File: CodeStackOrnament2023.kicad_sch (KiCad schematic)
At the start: 22 parts, among them SW1 SW_SPST, U1 NE555D, U2 4040

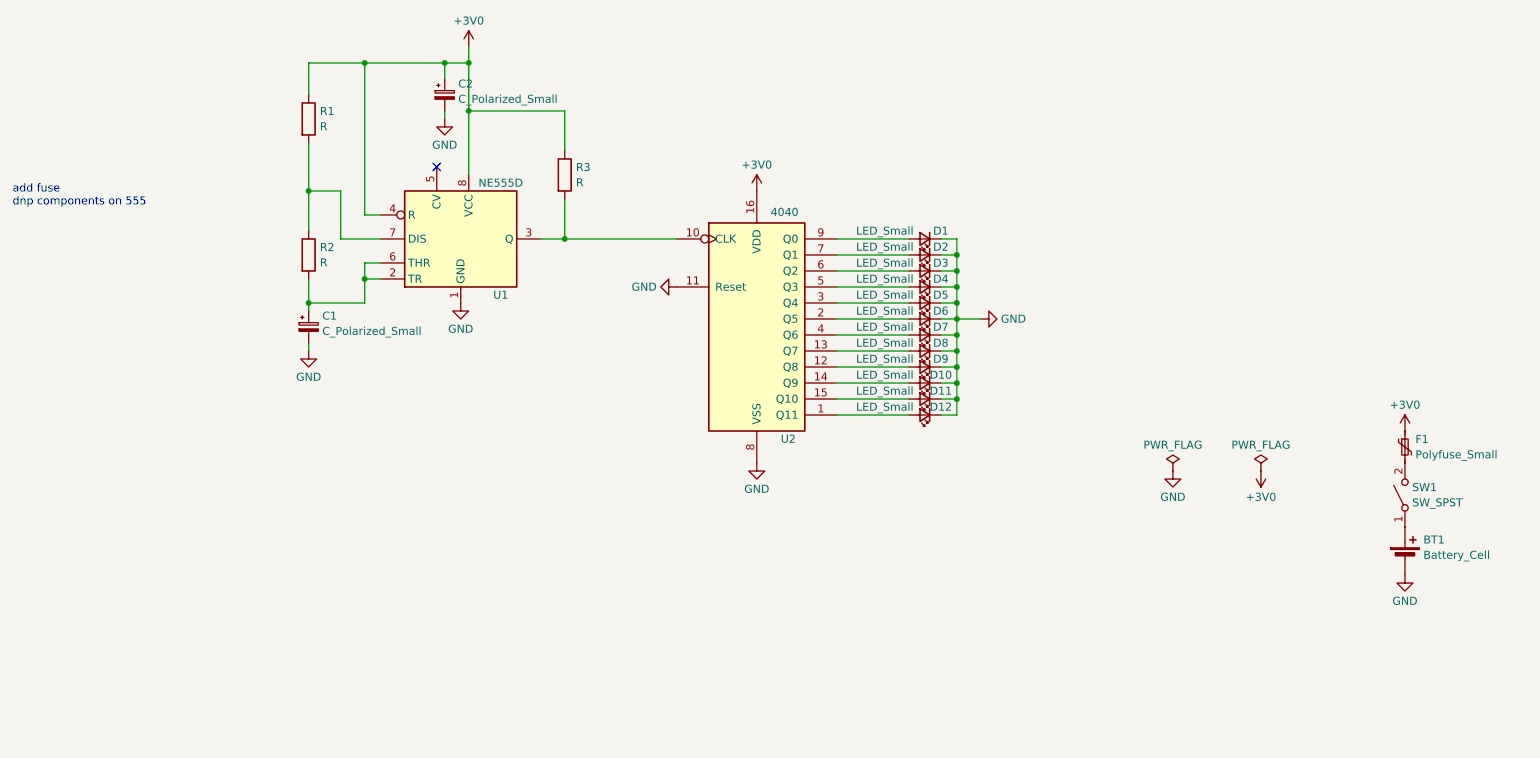
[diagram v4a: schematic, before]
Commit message: spice and footprint models. refactoring power supply.
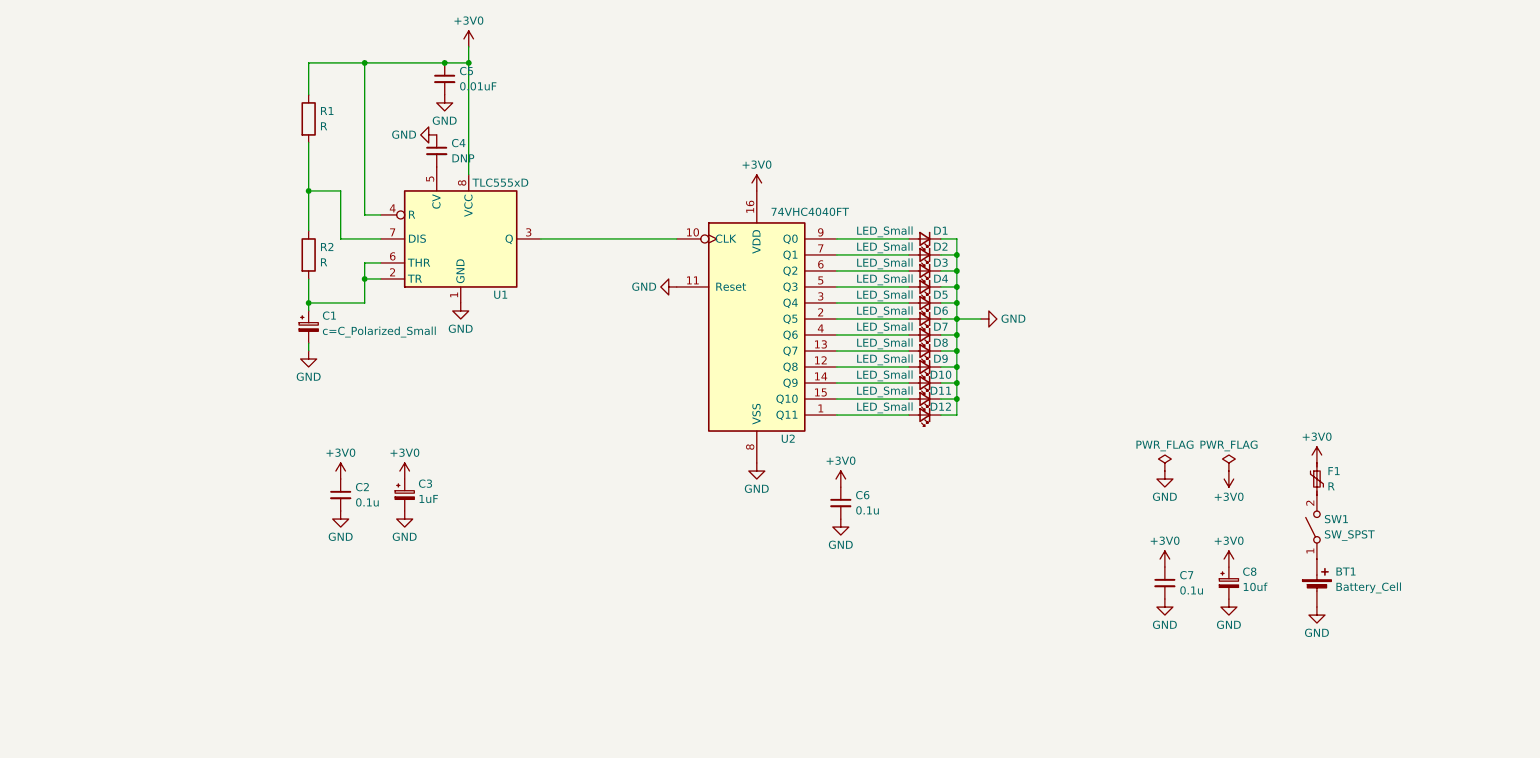
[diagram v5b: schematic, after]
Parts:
- removed C2: C_Polarized_Small, Capacitor_SMD:C_0805_2012Metric, symbol Device:C_Polarized_Small
- removed R3: R, Resistor_SMD:R_0805_2012Metric, symbol Device:R
- added C2, C6, C7: 0.1u, Capacitor_SMD:C_0805_2012Metric, symbol Device:C_Small
- added C3: 1uF, Capacitor_SMD:C_0805_2012Metric, symbol Device:C_Polarized_Small
- added C4: DNP, Capacitor_SMD:C_0805_2012Metric, symbol Device:C_Small
- added C5: 0.01uF, Capacitor_SMD:C_0805_2012Metric, symbol Device:C_Small
- added C8: 10uf, Capacitor_SMD:C_0805_2012Metric, symbol Device:C_Polarized_Small
- BT1: footprint CodeStackOrnament2023Footprints:2466_AAA_HOLDER -> CodeStackOrnament2023Footprints:BAT_2468
- C1: value C_Polarized_Small -> ${SIM.PARAMS}
- F1: value Polyfuse_Small -> R; footprint (none) -> Resistor_SMD:R_0805_2012Metric
- U1: value NE555D -> TLC555xD; footprint Package_SO:SOIC-8_3.9x4.9mm_P1.27mm -> CodeStackOrnament2023Footprints:TLC555_SOIC
- U2: value 4040 -> 74VHC4040FT
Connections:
- net +3V0: now also C2.1, C3.1, C5.1, C6.1, C7.1, C8.1
- net GND: now also C2.2, C3.2, C4.1, C5.2, C6.2, C7.2, C8.2
- net at U1.5 (CV): now also C4.2
- no-connect marks 1 -> 0
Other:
- note removed: "add fuse dnp components on 555"
- moved on the sheet: BT1, F1, SW1

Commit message: starting board design
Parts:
- removed C5: 0.01uF, Capacitor_SMD:C_0805_2012Metric, symbol Device:C_Small
- C1: value ${SIM.PARAMS} -> 10uF
- R1, R2: value R -> 8k
- renumbered C6 to C5, C7 to C6, C8 to C7
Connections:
- net at BT1.1 (+): now also SW1.2 (A); no longer SW1.1 (A)
- net at F1.2: now also SW1.3 (B); no longer SW1.2 (B)

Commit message: board layout
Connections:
- net +3V0: now also SW1.3 (B); no longer F1.1
- net at SW1.2 (A): now also F1.1; no longer BT1.1 (+)
- net at F1.2: now also BT1.1 (+); no longer SW1.3 (B)
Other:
- moved on the sheet: F1, SW1
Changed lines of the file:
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@@
     )
   )
-  (symbol (lib_id "Switch:SW_SPST") (at 229.87 97.79 90) (unit 1)
-    (in_bom yes) (on_board yes) (dnp no) (fields_autoplaced)
-    (property "Reference" "SW1" (at 231.013 96.5779 90)
+  (symbol (lib_id "Switch:SW_SPST") (at 229.87 92.71 90) (unit 1)
+    (in_bom yes) (on_board yes) (dnp no) (fields_autoplaced)
+    (property "Reference" "SW1" (at 231.013 91.4979 90)
       (effects (font (size 1.27 1.27)) (justify right))
     )
-    (property "Value" "SW_SPST" (at 231.013 99.0021 90)
+    (property "Value" "SW_SPST" (at 231.013 93.9221 90)
       (effects (font (size 1.27 1.27)) (justify right))
     )
-    (property "Footprint" "CodeStackOrnament2023Footprints:JS202011SCQN_SWITCH" (at 229.87 97.79 0)
-      (effects (font (size 1.27 1.27)) hide)
-    )
-    (property "Datasheet" "~" (at 229.87 97.79 0)
-      (effects (font (size 1.27 1.27)) hide)
-    )
-    (property "Sim.Device" "SW" (at 229.87 97.79 0)
-      (effects (font (size 1.27 1.27)) hide)
-    )
-    (property "Sim.Type" "V" (at 229.87 97.79 0)
-      (effects (font (size 1.27 1.27)) hide)
-    )
-    (property "Sim.Pins" "1=ctrl- 2=ctrl+" (at 229.87 97.79 0)
+    (property "Footprint" "CodeStackOrnament2023Footprints:JS202011SCQN_SWITCH" (at 229.87 92.71 0)
+      (effects (font (size 1.27 1.27)) hide)
+    )
+    (property "Datasheet" "~" (at 229.87 92.71 0)
+      (effects (font (size 1.27 1.27)) hide)
+    )
+    (property "Sim.Device" "SW" (at 229.87 92.71 0)
+      (effects (font (size 1.27 1.27)) hide)
+    )
+    (property "Sim.Type" "V" (at 229.87 92.71 0)
+      (effects (font (size 1.27 1.27)) hide)
+    )
+    (property "Sim.Pins" "1=ctrl- 2=ctrl+" (at 229.87 92.71 0)
       (effects (font (size 1.27 1.27)) hide)
     )
@@
     )
   )
-  (symbol (lib_id "Device:Polyfuse_Small") (at 229.87 90.17 0) (unit 1)
-    (in_bom yes) (on_board yes) (dnp no) (fields_autoplaced)
-    (property "Reference" "F1" (at 231.521 88.9579 0)
-      (effects (font (size 1.27 1.27)) (justify left))
-    )
-    (property "Value" "R" (at 231.521 91.3821 0)
-      (effects (font (size 1.27 1.27)) (justify left))
-    )
-    (property "Footprint" "Resistor_SMD:R_0805_2012Metric" (at 231.14 95.25 0)
+  (symbol (lib_id "Device:Polyfuse_Small") (at 229.87 100.33 0) (unit 1)
+    (in_bom yes) (on_board yes) (dnp no) (fields_autoplaced)
+    (property "Reference" "F1" (at 231.521 99.1179 0)
+      (effects (font (size 1.27 1.27)) (justify left))
+    )
+    (property "Value" "R" (at 231.521 101.5421 0)
+      (effects (font (size 1.27 1.27)) (justify left))
+    )
+    (property "Footprint" "Resistor_SMD:R_0805_2012Metric" (at 231.14 105.41 0)
       (effects (font (size 1.27 1.27)) (justify left) hide)
     )
-    (property "Datasheet" "~" (at 229.87 90.17 0)
-      (effects (font (size 1.27 1.27)) hide)
-    )
-    (property "Sim.Device" "R" (at 229.87 90.17 0)
-      (effects (font (size 1.27 1.27)) hide)
-    )
-    (property "Sim.Pins" "1=+ 2=-" (at 229.87 90.17 0)
-      (effects (font (size 1.27 1.27)) hide)
-    )
-    (property "Sim.Params" "r=\"\"" (at 229.87 90.17 0)
-      (effects (font (size 1.27 1.27)) hide)
-    )
+    (property "Datasheet" "~" (at 229.87 100.33 0)
+      (effects (font (size 1.27 1.27)) hide)
+    )
+    (property "Sim.Device" "R" (at 229.87 100.33 0)
+      (effects (font (size 1.27 1.27)) hide)
+    )
+    (property "Sim.Pins" "1=+ 2=-" (at 229.87 100.33 0)
+      (effects (font (size 1.27 1.27)) hide)
+    )
+    (property "Sim.Params" "r=\"\"" (at 229.87 100.33 0)
+      (effects (font (size 1.27 1.27)) hide)
+    )

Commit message: starting board routing
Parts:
- F1: footprint Resistor_SMD:R_0805_2012Metric -> CodeStackOrnament2023Footprints:SMD1206B050TF_FUSE
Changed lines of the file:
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@@
       (effects (font (size 1.27 1.27)) (justify left))
     )
-    (property "Footprint" "Resistor_SMD:R_0805_2012Metric" (at 231.14 105.41 0)
+    (property "Footprint" "CodeStackOrnament2023Footprints:SMD1206B050TF_FUSE" (at 231.14 105.41 0)
       (effects (font (size 1.27 1.27)) (justify left) hide)
     )
